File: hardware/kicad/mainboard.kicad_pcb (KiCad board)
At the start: 2 copper layers, 152.9 x 110.6 mm, 82 parts, among them J1 XT60PW, J10 Body NeoPixel, J11 Slip ring, J12 Charger XT30, J13 SPK L, J14 SPK R, J15 ESTOP, J16 I2C-A exp (ESP32), J17 I2C-B exp (RP2350), J2 DFR0601 ribbon 2x5, J3 DFR0601 ribbon 2x5, J4 Servo L, J5 Servo R, J6 IMU BMI160 SPI, J7 S2S AS5600/pot, J8 Dome encoder, J9 Hall, Q1 SQJ431EP P-FET RPP, U1 ESP-WROOM-32 DevKit 30p, U2 RP2350-Zero, U3 DFPlayer Mini, U5 AP7361C-33 3.3V LDO, U6 74AHCT125, U7 74LVC245A

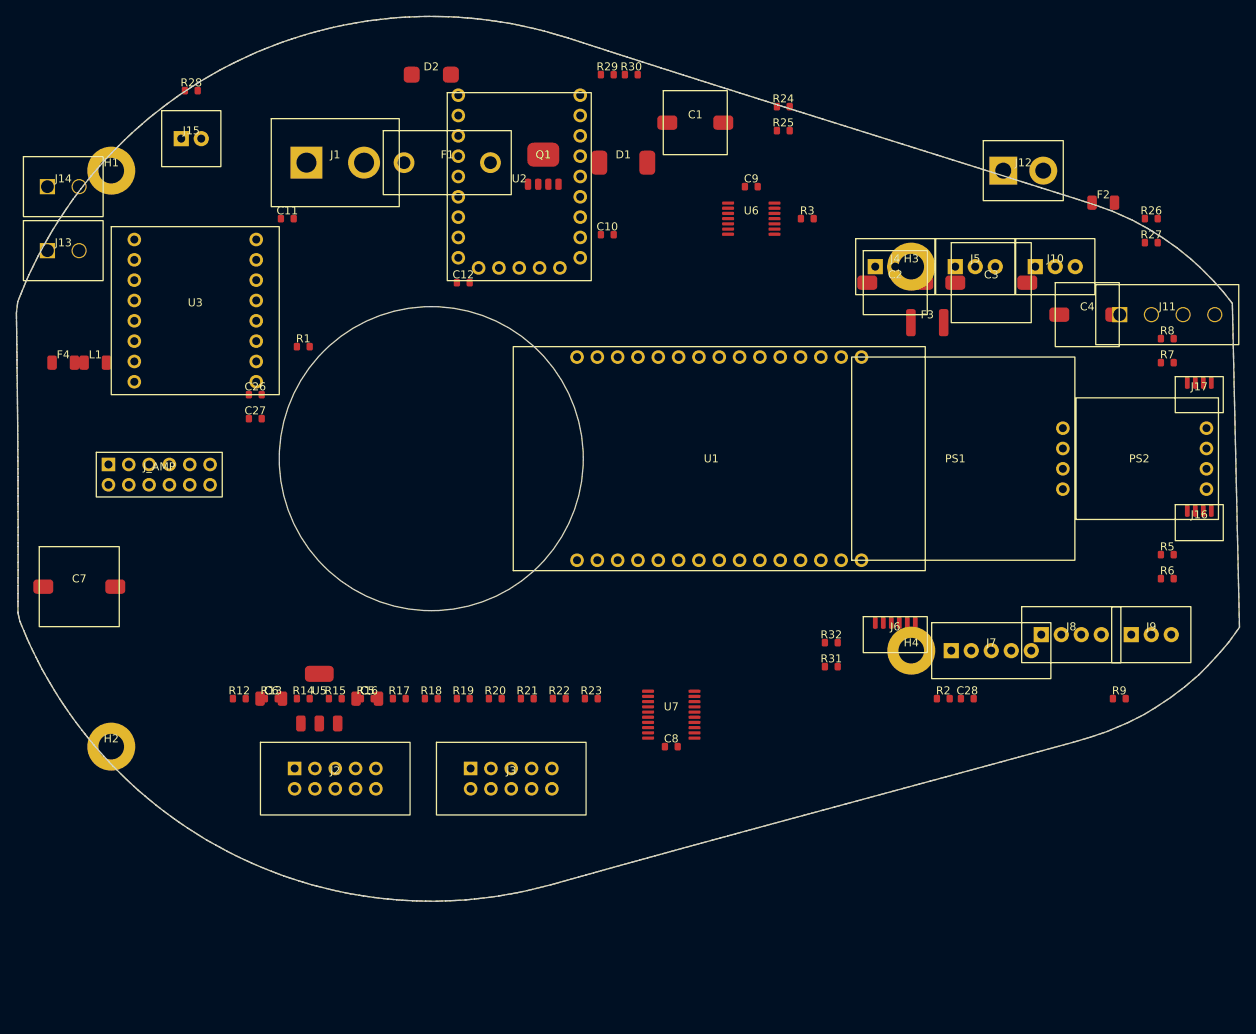
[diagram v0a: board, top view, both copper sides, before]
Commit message: v10 KiCad mainboard: collision-aware placer, library footprints, ERC 0 errors, placed on the casing outline; boss coordinates for the casing model
Co-Authored-By: Claude Opus 5 (1M context) <noreply@anthropic.com>
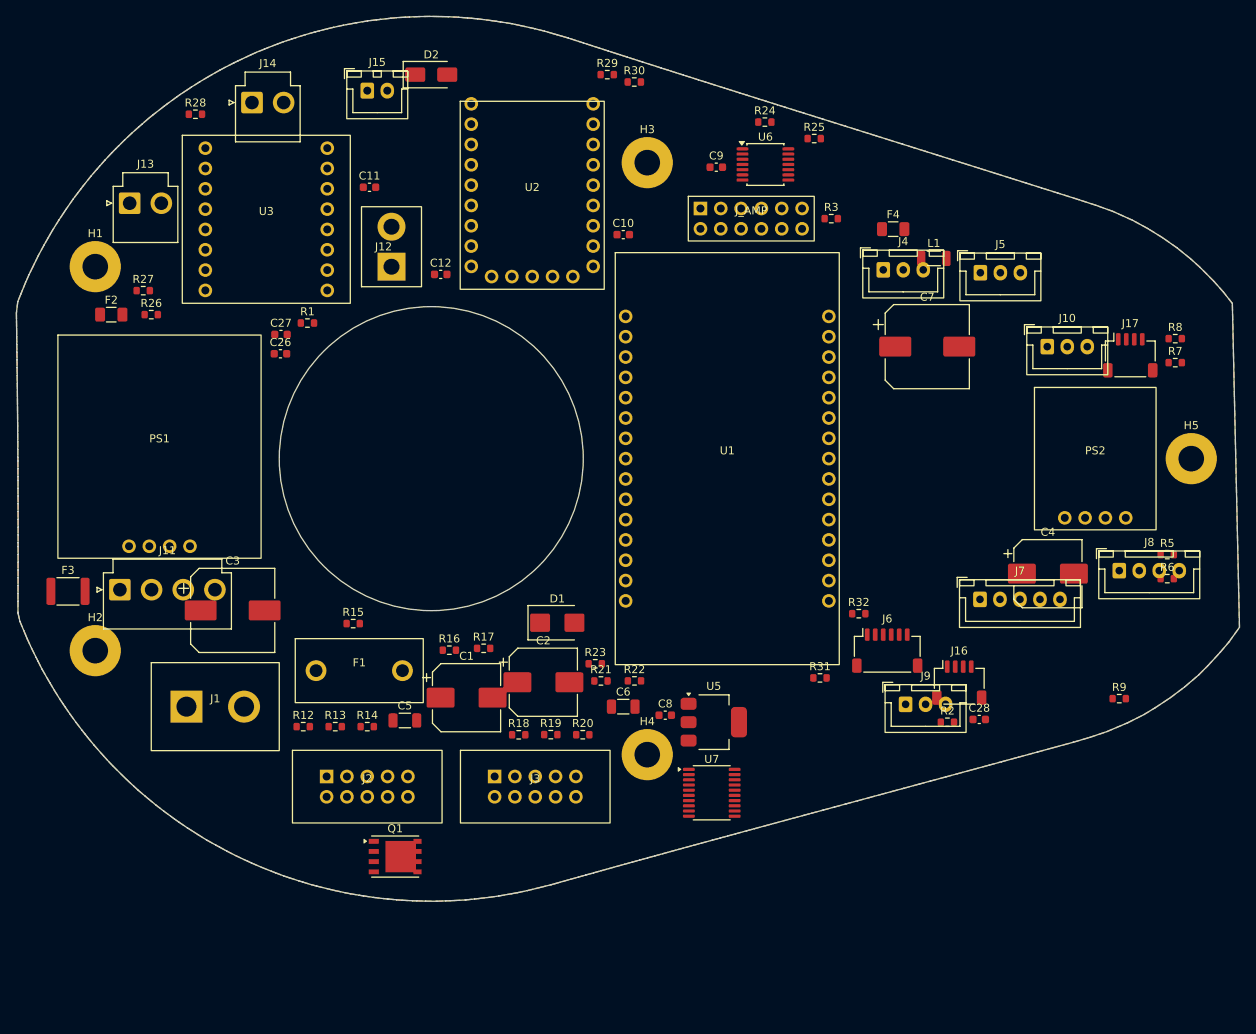
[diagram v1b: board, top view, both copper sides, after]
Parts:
- added H5: M3 boss, MountingHole_3.2mm_M3_Pad, F.Cu at (245.0, 150.0)
- C1, C2, C4: footprint Capacitor_SMD:CP_Elec_8x10 -> CP_Elec_8x10
- C10, C11, C12, C26, C27, C28, C8, C9: footprint Capacitor_SMD:C_0603_1608Metric -> C_0603_1608Metric
- C3, C7: footprint Capacitor_SMD:CP_Elec_10x10 -> CP_Elec_10x10
- C5, C6: footprint Capacitor_SMD:C_1206_3216Metric -> C_1206_3216Metric
- D1: footprint Diode_SMD:D_SMB -> D_SMB
- D2: footprint Diode_SMD:D_SMA -> D_SMA
- F2, F4: footprint Fuse:Fuse_1206_3216Metric -> Fuse_1206_3216Metric
- F3: footprint Fuse:Fuse_1812_4532Metric -> Fuse_1812_4532Metric
- H1, H2, H3, H4: footprint MountingHole:MountingHole_3.2mm_M3_Pad -> MountingHole_3.2mm_M3_Pad
- J10, J4, J5, J9: footprint Connector_JST:JST_XH_B3B-XH-A_1x03_P2.50mm_Vertical -> JST_XH_B3B-XH-A_1x03_P2.50mm_Vertical
- J11: footprint Connector_JST:JST_VH_B4P-VH_1x04_P3.96mm_Vertical -> JST_VH_B4P-VH_1x04_P3.96mm_Vertical
- J13, J14: footprint Connector_JST:JST_VH_B2P-VH_1x02_P3.96mm_Vertical -> JST_VH_B2P-VH_1x02_P3.96mm_Vertical
- J15: footprint Connector_JST:JST_XH_B2B-XH-A_1x02_P2.50mm_Vertical -> JST_XH_B2B-XH-A_1x02_P2.50mm_Vertical
- J16, J17: footprint Connector_JST:JST_SH_SM04B-SRSS-TB_1x04-1MP_P1.00mm_Horizontal -> JST_SH_SM04B-SRSS-TB_1x04-1MP_P1.00mm_Horizontal
- J6: footprint Connector_JST:JST_SH_SM06B-SRSS-TB_1x06-1MP_P1.00mm_Horizontal -> JST_SH_SM06B-SRSS-TB_1x06-1MP_P1.00mm_Horizontal
- J7: footprint Connector_JST:JST_XH_B5B-XH-A_1x05_P2.50mm_Vertical -> JST_XH_B5B-XH-A_1x05_P2.50mm_Vertical
- J8: footprint Connector_JST:JST_XH_B4B-XH-A_1x04_P2.50mm_Vertical -> JST_XH_B4B-XH-A_1x04_P2.50mm_Vertical
- L1: footprint Inductor_SMD:L_1206_3216Metric -> L_1206_3216Metric
- Q1: footprint Package_SO:PowerPAK_SO-8_Single -> PowerPAK_SO-8_Single
- R1, R12, R13, R14, R15, R16, R17, R18, R19, R2, R20, R21, R22, R23, R24, R25, R26, R27, R28, R29, R3, R30, R31, R32, R5, R6, R7, R8, R9: footprint Resistor_SMD:R_0603_1608Metric -> R_0603_1608Metric
- U5: footprint Package_TO_SOT_SMD:SOT-223-3_TabPin2 -> SOT-223-3_TabPin2
- U6: footprint Package_SO:TSSOP-14_4.4x5mm_P0.65mm -> TSSOP-14_4.4x5mm_P0.65mm
- U7: footprint Package_SO:TSSOP-20_4.4x6.5mm_P0.65mm -> TSSOP-20_4.4x6.5mm_P0.65mm
- moved J11 135.4 mm to (111.1, 166.4)
- moved R27 126.1 mm to (114.0, 129.0)
- moved R26 125.6 mm to (115.0, 132.0)
- moved F2 124.8 mm to (110.0, 132.0)
- moved F3 112.5 mm to (104.6, 166.6)
- moved C7 110.2 mm to (212.0, 136.0)
- moved L1 105.6 mm to (212.8, 125.0)
- moved F4 105.1 mm to (207.7, 121.3)
- moved C3 103.3 mm to (125.2, 169.0)
- moved PS1 100.5 mm to (116.0, 148.5), turned to 0 degrees
- moved Q1 88.7 mm to (145.5, 199.7)
- moved J_AMP 80.6 mm to (190.0, 120.0)
- moved J12 79.5 mm to (145.0, 123.5), turned to 90 degrees
- moved C1 77.4 mm to (154.4, 179.9)
- moved J1 69.6 mm to (123.0, 181.0)
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
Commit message: v10 mainboard: true 2 mm outline offset (was 0.95 mm min), DFPlayer at tail tip with SD slot facing the opening, 6 V buck to left lobe, board title + credits on silkscreen, schematic title block; renders in docs
Co-Authored-By: Claude Opus 5 (1M context) <noreply@anthropic.com>
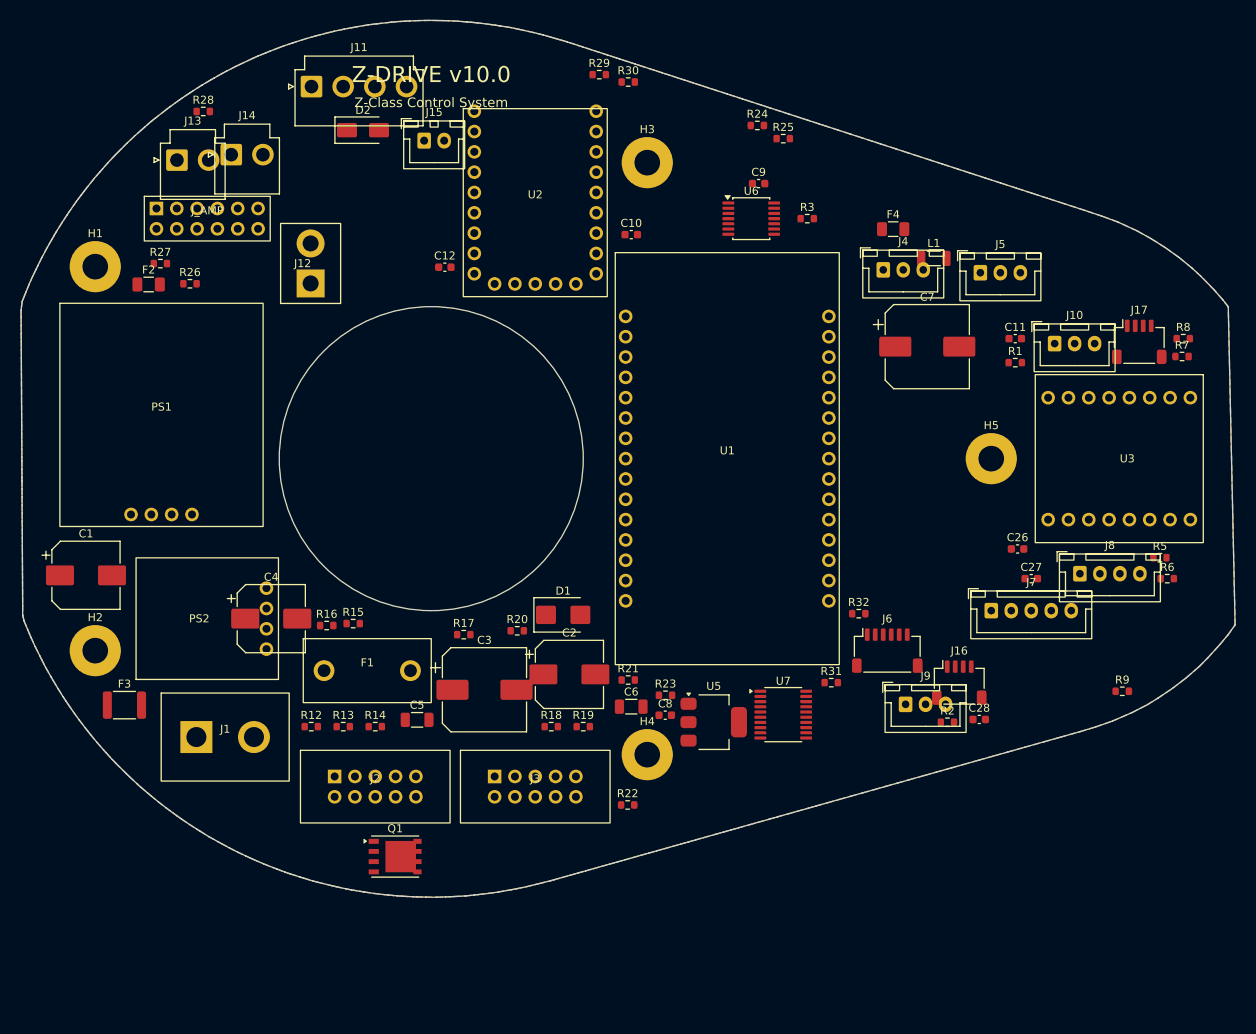
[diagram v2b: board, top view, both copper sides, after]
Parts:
- moved PS2 112.8 mm to (122.0, 170.0), turned to 90 degrees
- moved U3 110.7 mm to (236.0, 150.0), turned to 270 degrees
- moved C27 98.6 mm to (225.0, 165.0)
- moved C4 97.2 mm to (130.0, 170.0)
- moved C26 95.3 mm to (223.3, 161.3)
- moved R1 88.6 mm to (223.0, 138.0)
- moved C11 82.9 mm to (223.0, 135.0)
- moved J_AMP 68.0 mm to (122.0, 120.0)
- moved J11 67.3 mm to (135.0, 103.5)
- moved C1 50.0 mm to (106.8, 164.6)
- moved C3 33.0 mm to (156.7, 178.9)
- moved H5 25.0 mm to (220.0, 150.0)
- moved F3 15.9 mm to (111.7, 180.8)
- moved R16 15.6 mm to (136.9, 170.9)
- moved R22 15.5 mm to (174.6, 193.3)
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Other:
- board size 152.9 x 110.6 mm -> 151.8 x 109.6 mm
- board text added: "Design by James VanDusen"
- board text added: "Special thanks to Mimir Reynisson, Greg Bellows and Joe Latiola"
- board text added: "Z-Class Control System"
- board text added: "Z-DRIVE v10.0"
- board text added: "Z-DRIVE v10.0 MAINBOARD"
- board text added: "github.com/jlvandusen/Z-ClassControlSystem"
- board text added: "rev A 221b7d0 2026-08-21"

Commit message: v10 mainboard: DevKit right-column pinout corrected (3V3 at USB end), ESP32 antenna copper keep-out, 31 GND stitching vias, current-based netclasses (Power 3.0 mm, Audio 1.0, Motor 0.5), 10 A input fuse
Co-Authored-By: Claude Opus 5 (1M context) <noreply@anthropic.com>
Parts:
- F1: value 15A blade fuse -> 10A blade fuse
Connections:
- U1 pad 16: (no net) -> IMU_MOSI
- U1 pad 17: GND -> LINK_RP_TX
- U1 pad 18: I2C_A_SCL -> (no net)
- U1 pad 20: DRIVE_PWM -> LINK_ESP_TX
- U1 pad 21: DRIVE_INA -> IMU_MISO
- U1 pad 22: DRIVE_INB -> IMU_SCK
- U1 pad 24: IMU_SCK -> DRIVE_INB
- U1 pad 25: IMU_MISO -> DRIVE_INA
- U1 pad 26: LINK_ESP_TX -> DRIVE_PWM
- U1 pad 28: (no net) -> I2C_A_SCL
- U1 pad 29: LINK_RP_TX -> GND
- U1 pad 30: IMU_MOSI -> (no net)
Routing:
- net GND: vias 0 -> 31
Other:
- board text added: "rev A 810a2a2 2026-08-21"
- board text removed: "rev A 221b7d0 2026-08-21"

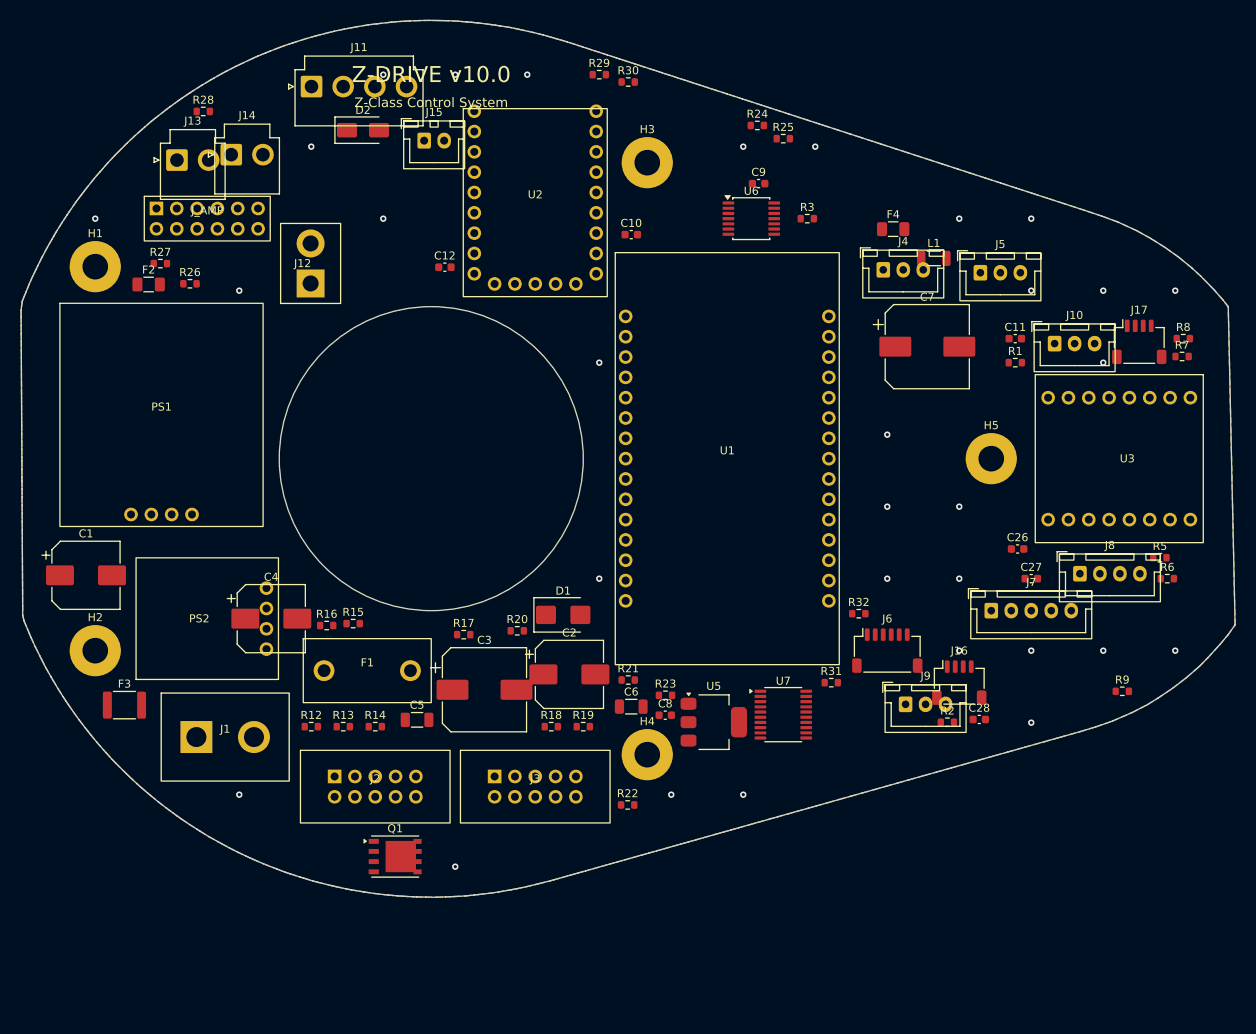
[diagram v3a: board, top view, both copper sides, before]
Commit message: v10 mainboard: 4-layer (In1 GND plane, In2 +5V plane), autorouted ~90% (Freerouting 2.3), stitching + planes; remaining opens/edge-clearances are manual GUI finishing
Co-Authored-By: Claude Opus 5 (1M context) <noreply@anthropic.com>
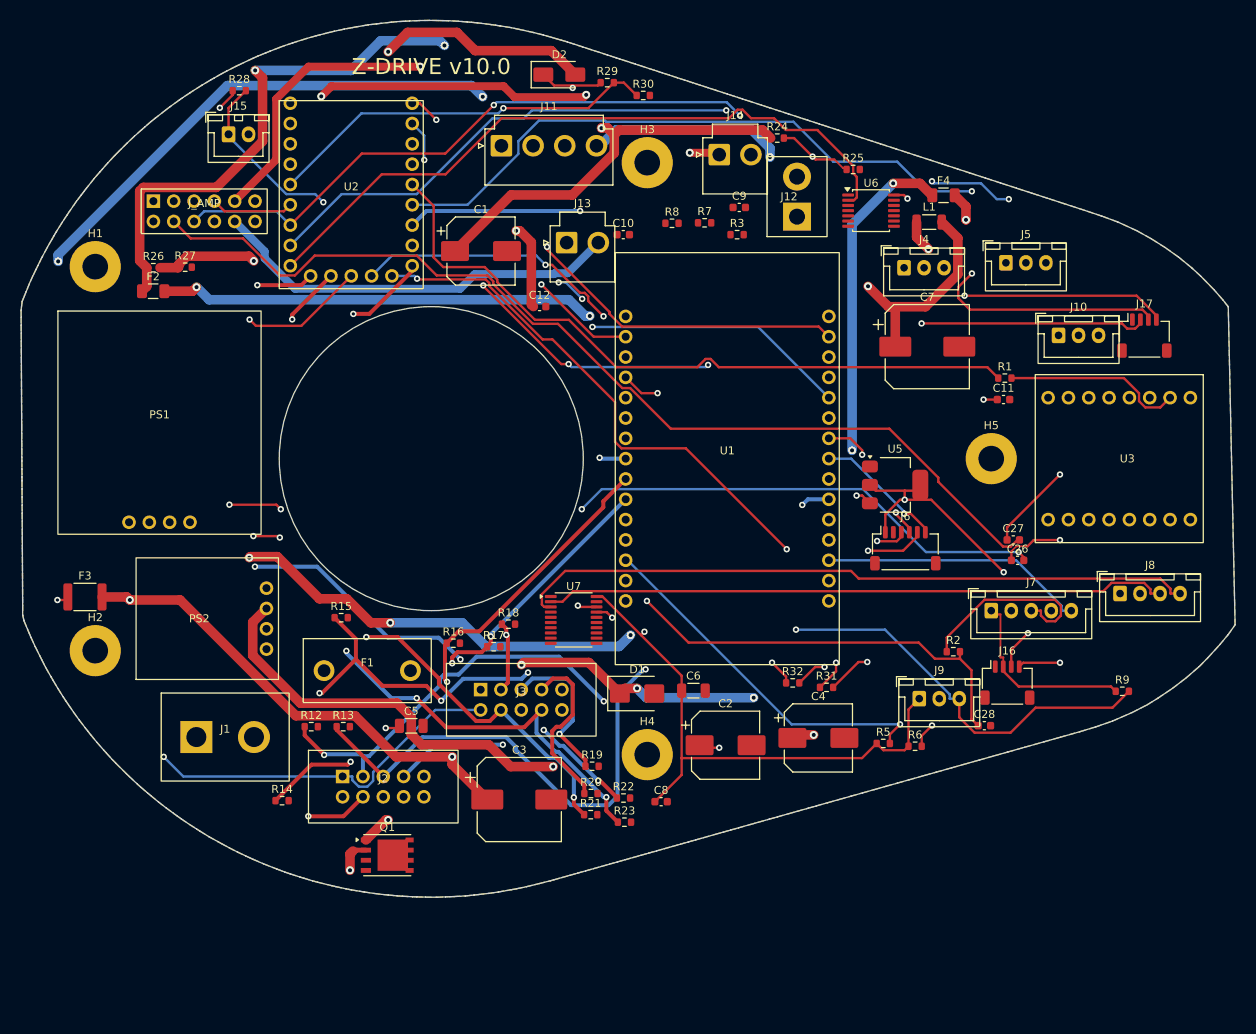
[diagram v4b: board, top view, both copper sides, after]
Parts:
- moved C4 70.0 mm to (198.4, 184.9)
- moved R8 65.5 mm to (180.1, 120.6)
- moved C1 63.9 mm to (156.2, 124.0)
- moved R7 62.0 mm to (184.2, 120.5)
- moved J12 61.4 mm to (195.7, 117.2)
- moved J14 61.0 mm to (186.0, 112.0)
- moved J13 49.8 mm to (166.9, 123.0)
- moved R5 41.7 mm to (206.5, 185.6)
- moved R6 37.8 mm to (210.5, 185.9)
- moved U5 37.3 mm to (208.0, 153.3)
- moved U7 28.8 mm to (167.8, 170.2)
- moved D2 25.5 mm to (166.0, 102.0)
- moved J11 24.9 mm to (158.8, 110.9)
- moved J15 24.5 mm to (124.7, 109.5)
- moved U2 23.0 mm to (140.0, 117.0)
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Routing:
- net +3V3: track 0.00 -> 366.3 mm, vias 0 -> 6
- net VIN: track 0.00 -> 362.6 mm, vias 0 -> 7
- net +5V_LED: track 0.00 -> 284.2 mm, vias 0 -> 4
- net +6V_SERVO: track 0.00 -> 189.7 mm, vias 0 -> 2
- net AMP_12V: track 0.00 -> 188.3 mm, vias 0 -> 4
- net AMP_INL: track 0.00 -> 158.8 mm, vias 0 -> 4
- net DF_BUSY: track 0.00 -> 151.0 mm, vias 0 -> 3
- net I2C_B_SDA: track 0.00 -> 147.2 mm, vias 0 -> 3
- net I2C_B_SCL: track 0.00 -> 134.1 mm, vias 0 -> 4
- net HALL: track 0.00 -> 128.0 mm, vias 0 -> 3
- net AMP_INR: track 0.00 -> 125.5 mm
- net DF_RX_RP: track 0.00 -> 115.2 mm, vias 0 -> 1
- net DOME_INA: track 0.00 -> 104.5 mm, vias 0 -> 5
- net DOME_INB: track 0.00 -> 102.7 mm, vias 0 -> 4
- net DOME_PWM: track 0.00 -> 99.7 mm, vias 0 -> 3
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- added copper zone on In2.Cu, net +5V_LOGIC
- added copper zone on In1.Cu, net GND
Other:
- copper layers 2 -> 4
- board text added: "rev A 34f1afa 2026-08-21"
- board text removed: "Z-Class Control System"
- board text removed: "rev A 810a2a2 2026-08-21"

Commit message: v10 mainboard: 4-layer routed ~95% (F/B GND pours + In1 GND/In2 +5V planes), 7.4V servo rail (D24V25F7); 27 signal/plane opens + 11 edge tracks remain for interactive GUI finish
Co-Authored-By: Claude Opus 5 (1M context) <noreply@anthropic.com>
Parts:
- C4: value 470u/10V -> 470u/16V
- PS2: value Pololu D24V22F6 6V 2.5A -> Pololu D24V25F7 7.5V 2.5A
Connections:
- net +6V_SERVO renamed +7V4_SERVO
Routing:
- net ENC_A_3V3: track 92.0 -> 0.00 mm, vias 4 -> 0
- net SERVO_R: track 0.00 -> 90.1 mm, vias 0 -> 1
- net DF_TX_RP: track 88.1 -> 0.00 mm
- net VIN: track 362.6 -> 276.4 mm, vias 7 -> 5
- net ENC_B_5V: track 85.0 -> 0.00 mm
- net AMP_12V: track 188.3 -> 249.1 mm, vias 4 -> 6
- net ESTOP_SENSE: track 66.6 -> 6.36 mm, vias 2 -> 0
- net +5V_LED: track 284.2 -> 318.0 mm
- net AMP_INL: track 158.8 -> 128.0 mm, vias 4 -> 2
- net DF_BUSY: track 151.0 -> 127.7 mm, vias 3 -> 1
- net SERVO_L: track 75.2 -> 92.2 mm
- net S2S_PWM: track 95.8 -> 81.0 mm, vias 5 -> 2
- net DRIVE_INA: track 93.9 -> 79.3 mm, vias 2 -> 0
- net I2C_B_SDA: track 147.2 -> 133.2 mm, vias 3 -> 0
- net ENC_B_3V3: track 81.4 -> 68.1 mm, vias 3 -> 1
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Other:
- board text added: "rev A 00f3452 2026-08-21"
- board text removed: "rev A 34f1afa 2026-08-21"
